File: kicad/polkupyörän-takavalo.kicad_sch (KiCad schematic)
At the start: 15 parts, among them J1 Conn_01x06_Pin, SW1 SW_Push, U1 STM32G030F6Px

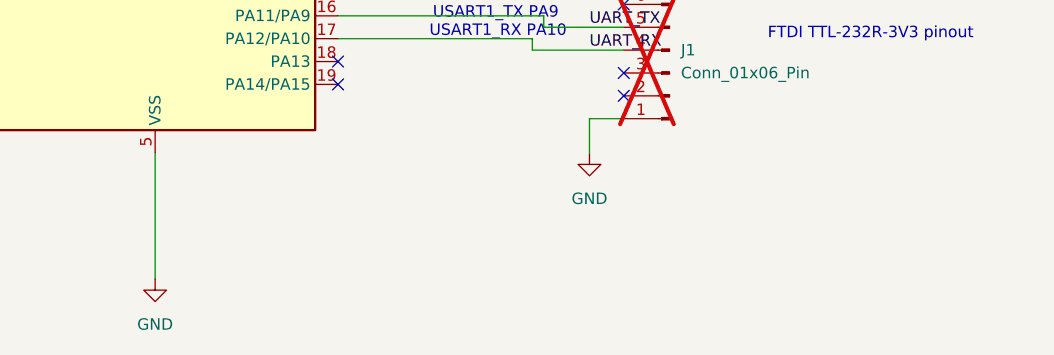
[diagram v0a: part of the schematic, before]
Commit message: Light off the led before going to sleep
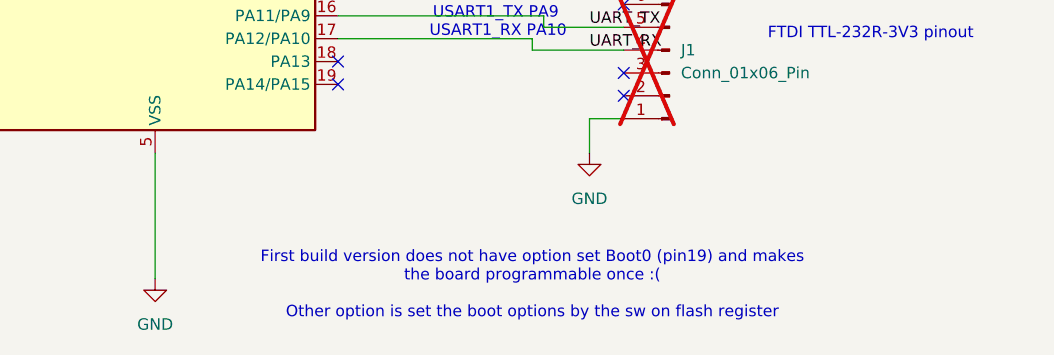
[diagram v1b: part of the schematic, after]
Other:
- note added: "First build version does not have option set Boot0 (pin19) and makes the board programmable once :( Other option is set the boot options by the sw on flash register"
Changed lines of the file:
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@@
+		)
+	)
+	(text "First build version does not have option set Boot0 (pin19) and makes \nthe board programmable once :( \n\nOther option is set the boot options by the sw on flash register "
+		(exclude_from_sim no)
+		(at 200.66 137.922 0)
+		(effects
+			(font
+				(size 1.27 1.27)
+			)
 		)
 	)
